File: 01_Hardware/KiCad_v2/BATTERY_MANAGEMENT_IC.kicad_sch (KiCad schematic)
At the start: 36 parts, among them J300 JST_B2B, Q300 BSS314PE, Q301 NVTA7002NT1G, U300 BQ25892

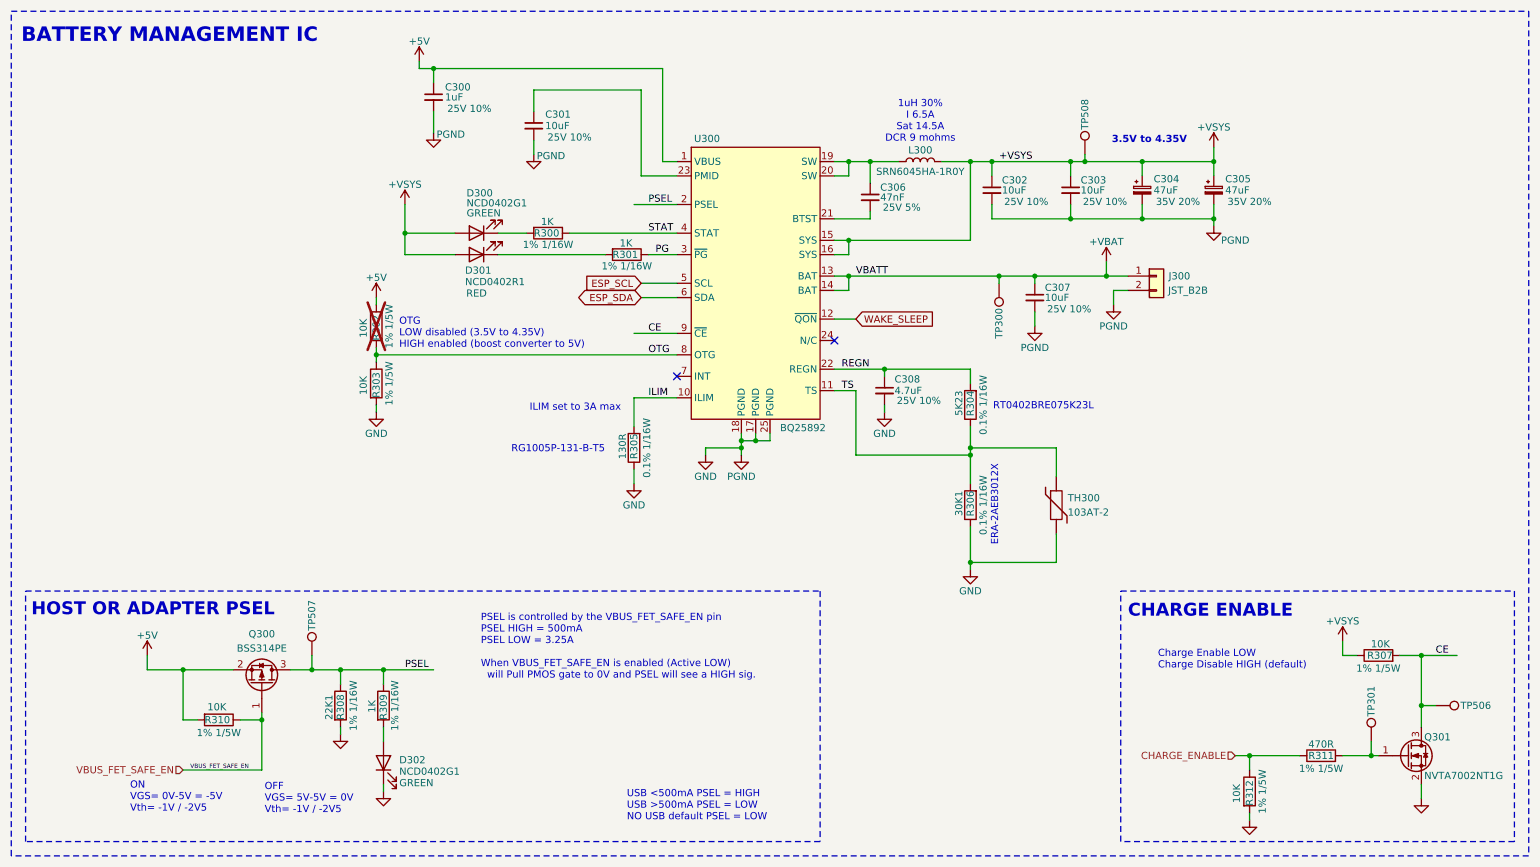
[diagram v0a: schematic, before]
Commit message: BOM done, except connectors/thermistor/button -> Will re-check BOM before sending to manufacturing
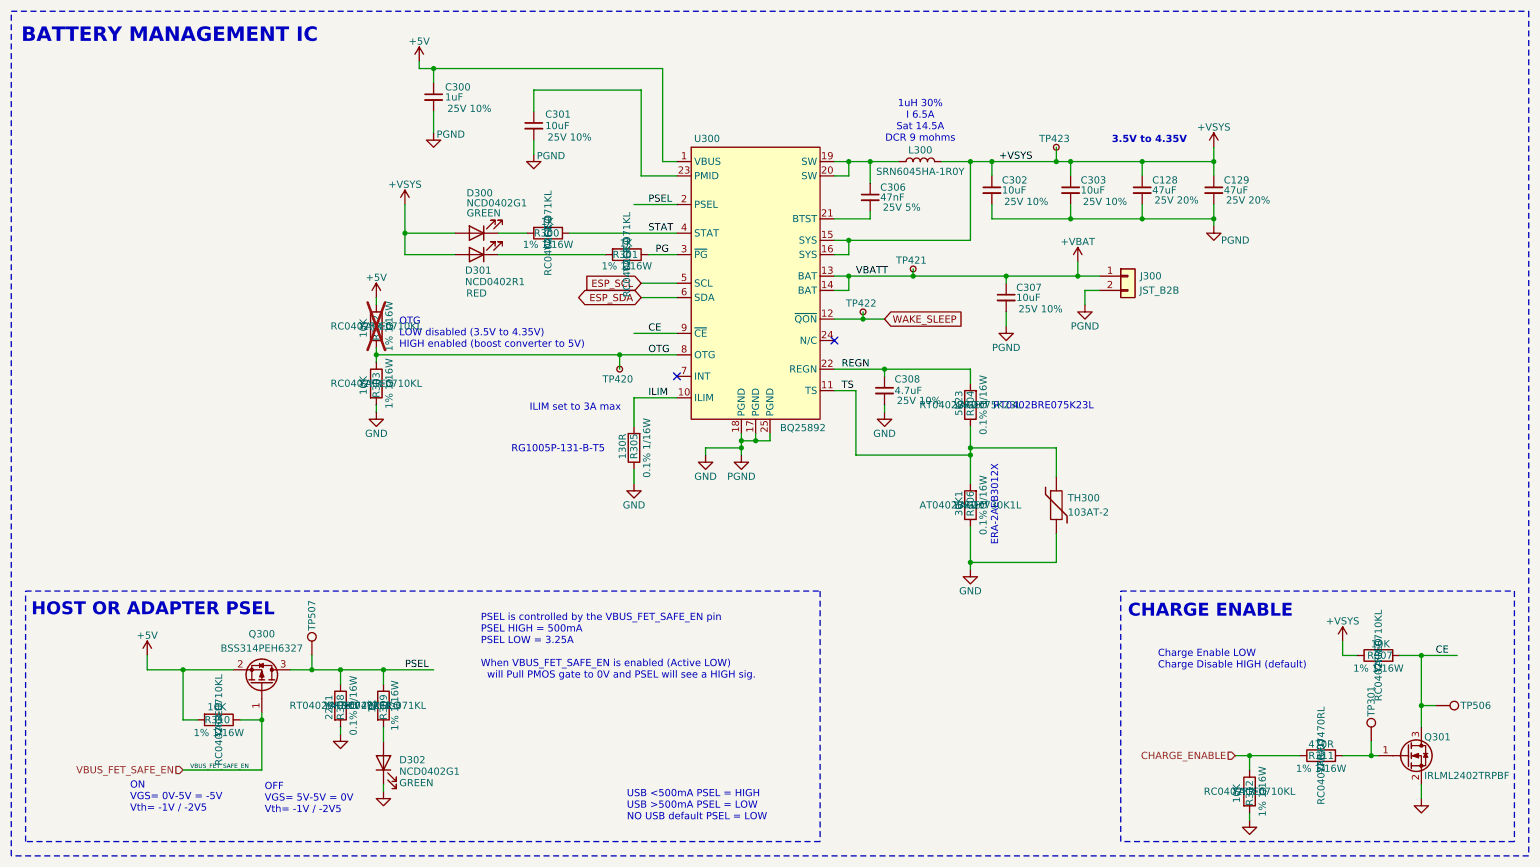
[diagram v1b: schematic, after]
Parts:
- removed C304, C305: 47uF, Capacitor_SMD:CP_Elec_6.3x5.8, symbol Device:C_Polarized_Small
- removed TP300: +VBAT, TestPoint:TestPoint_Pad_D1.0mm, symbol Connector:TestPoint
- removed TP508: ~, TestPoint:TestPoint_Pad_D1.0mm, symbol Connector:TestPoint
- added C128, C129: 47uF, Capacitor_SMD:C_1206_3216Metric, symbol Device:C_Small
- added TP420, TP421, TP422, TP423: TestPoint_Small, TestPoint:TestPoint_Pad_D1.5mm, symbol Connector:TestPoint_Small
- C301, C302, C303, C307: Manufacturer Murata Electronics -> Murata Electronics
- D300, D301, D302: footprint Custom_Global_Footprints:SML-P13PTT_LED_0402_1005Metric -> LED_SMD:LED_0402_1005Metric
- Q300: value BSS314PE -> BSS314PEH6327; Link (none) -> https://jlcpcb.com/partdetail/InfineonTechnologies-BSS314PE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; Manufacturer (none) -> Infineon Technologies; Manufacturer Part Number (none) -> BSS314PEH6327
- Q301: value NVTA7002NT1G -> IRLML2402TRPBF; footprint Custom_Global_Footprints:NVTA7002N -> Package_TO_SOT_SMD:SOT-23; Link (none) -> https://jlcpcb.com/partdetail/InfineonTechnologies-IRLML240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; Manufacturer (none) -> Infineon Technologies; Manufacturer Part Number (none) -> IRLML2402TRPBF
- R300, R301, R309: Manufacturer (none) -> YAGEO; Manufacturer Part Number (none) -> RC0402FR-071KL
- R302, R303, R307, R310, R312: Manufacturer (none) -> YAGEO; Manufacturer Part Number (none) -> RC0402FR-0710KL
- R304: Manufacturer (none) -> YAGEO; Manufacturer Part Number (none) -> RT0402BRD075K23L
- R305: Manufacturer (none) -> YAGEO; Manufacturer Part Number (none) -> RT0402BRD07130RL
- R306: Manufacturer (none) -> YAGEO; Manufacturer Part Number (none) -> AT0402BRD0730K1L
- R308: Manufacturer (none) -> YAGEO; Manufacturer Part Number (none) -> RT0402BRD0722K1L
- R311: Manufacturer (none) -> YAGEO; Manufacturer Part Number (none) -> RC0402FR-07470RL
- U300: Link (none) -> https://jlcpcb.com/partdetail/TexasInstruments-BQ25892RTWR/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; Manufacturer (none) -> Texas Instruments; Manufacturer Part Number (none) -> BQ25892RTWR
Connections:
- net +VBAT: now also TP421.1
- net +VSYS: now also C128.1, C129.1, TP423.1
- net GND: now also C128.2, C129.2
- net OTG: now also TP420.1
- net WAKE_SLEEP: now also TP422.1
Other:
- moved on the sheet: C307, J300

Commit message: USB-C and Serial PCB routing done
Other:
- note removed: "ERA-2AEB3012X"
- note removed: "RT0402BRE075K23L"
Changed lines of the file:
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@@
 		)
 	)
-	(text "RT0402BRE075K23L"
-		(exclude_from_sim no)
-		(at 197.104 84.074 0)
-		(effects
-			(font
-				(size 1.27 1.27)
-			)
-		)
-	)
 	(text "PSEL is controlled by the VBUS_FET_SAFE_EN pin\nPSEL HIGH = 500mA\nPSEL LOW = 3.25A\n\nWhen VBUS_FET_SAFE_EN is enabled (Active LOW)\n  will Pull PMOS gate to 0V and PSEL will see a HIGH sig."
 		(exclude_from_sim no)
@@
 		)
 	)
-	(text "ERA-2AEB3012X"
-		(exclude_from_sim no)
-		(at 188.468 101.6 90)
-		(effects
-			(font
-				(size 1.27 1.27)
-			)
-		)
-	)
 	(text "ON\nVGS= 0V-5V = -5V\nVth= -1V / -2V5"
 		(exclude_from_sim no)
@@
 					(size 1.27 1.27)
 				)
+				(hide yes)
 			)
 		)
@@
 					(size 1.27 1.27)
 				)
+				(hide yes)
 			)
 		)
@@
 					(size 1.27 1.27)
 				)
+				(hide yes)
 			)
 		)
@@
 					(size 1.27 1.27)
 				)
+				(hide yes)
 			)
 		)
@@
 					(size 1.27 1.27)
 				)
+				(hide yes)
 			)
 		)
@@
 					(size 1.27 1.27)
 				)
+				(hide yes)
 			)
 		)
@@
 					(size 1.27 1.27)
 				)
+				(hide yes)
 			)
 		)
@@
 					(size 1.27 1.27)
 				)
+				(hide yes)
 			)
 		)
@@
 					(size 1.27 1.27)
 				)
+				(hide yes)
 			)
 		)
@@
 					(size 1.27 1.27)
 				)
+				(hide yes)
 			)
 		)
@@
 					(size 1.27 1.27)
 				)
+				(hide yes)
 			)
 		)
@@
 					(size 1.27 1.27)
 				)
+				(hide yes)
 			)
 		)
@@
 					(size 1.27 1.27)
 				)
+				(hide yes)
 			)
 		)
@@
 					(size 1.27 1.27)
 				)
+				(hide yes)
 			)
 		)
@@
 					(size 1.27 1.27)
 				)
+				(hide yes)
 			)
 		)
@@
 					(size 1.27 1.27)
 				)
+				(hide yes)
 			)
 		)
@@
 					(size 1.27 1.27)
 				)
+				(hide yes)
 			)
 		)
@@
 					(size 1.27 1.27)
 				)
+				(hide yes)
 			)
 		)
@@
 					(size 1.27 1.27)
 				)
+				(hide yes)
 			)
 		)
@@
 					(size 1.27 1.27)
 				)
+				(hide yes)
 			)
 		)
@@
 					(size 1.27 1.27)
 				)
+				(hide yes)
 			)
 		)
@@
 					(size 1.27 1.27)
 				)
+				(hide yes)
 			)
 		)
@@
 					(size 1.27 1.27)
 				)
+				(hide yes)
 			)
 		)
@@
 					(size 1.27 1.27)
 				)
+				(hide yes)
 			)
 		)
@@
 					(size 1.27 1.27)
 				)
+				(hide yes)
 			)
 		)
@@
 					(size 1.27 1.27)
 				)
+				(hide yes)
 			)
 		)
@@
 					(size 1.27 1.27)
 				)
+				(hide yes)
 			)
 		)
@@
 					(size 1.27 1.27)
 				)
+				(hide yes)
 			)
 		)
@@
 					(size 1.27 1.27)
 				)
+				(hide yes)
 			)
 		)
@@
 					(size 1.27 1.27)
 				)
+				(hide yes)
 			)
 		)
@@
 					(size 1.27 1.27)
 				)
+				(hide yes)
 			)
 		)
@@
 					(size 1.27 1.27)
 				)
+				(hide yes)
 			)
 		)
@@
 					(size 1.27 1.27)
 				)
+				(hide yes)
 			)
 		)
@@
 					(size 1.27 1.27)
 				)
+				(hide yes)
 			)
 		)
@@
 					(size 1.27 1.27)
 				)
+				(hide yes)
 			)
 		)
@@
 					(size 1.27 1.27)
 				)
+				(hide yes)
 			)
 		)
@@
 					(size 1.27 1.27)
 				)
+				(hide yes)
 			)
 		)
@@
 					(size 1.27 1.27)
 				)
+				(hide yes)
 			)
 		)
@@
 					(size 1.27 1.27)
 				)
+				(hide yes)
 			)
 		)
@@
 					(size 1.27 1.27)
 				)
+				(hide yes)
 			)
 		)
@@
 					(size 1.27 1.27)
 				)
+				(hide yes)
 			)
 		)
@@
 					(size 1.27 1.27)
 				)
+				(hide yes)
 			)
 		)
@@
 					(size 1.27 1.27)
 				)
+				(hide yes)
 			)
 		)
@@
 					(size 1.27 1.27)
 				)
+				(hide yes)
 			)
 		)
@@
 					(size 1.27 1.27)
 				)
+				(hide yes)
 			)
 		)
@@
 					(size 1.27 1.27)
 				)
+				(hide yes)
 			)
 		)
@@
 					(size 1.27 1.27)
 				)
+				(hide yes)
 			)
 		)
@@
 					(size 1.27 1.27)
 				)
+				(hide yes)
 			)
 		)
@@
 					(size 1.27 1.27)
 				)
+				(hide yes)
 			)
 		)
@@
 					(size 1.27 1.27)
 				)
+				(hide yes)
 			)
 		)
@@
 					(size 1.27 1.27)
 				)
+				(hide yes)
 			)
 		)
@@
 					(size 1.27 1.27)
 				)
+				(hide yes)
 			)
 		)
@@
 					(size 1.27 1.27)
 				)
+				(hide yes)
 			)
 		)
@@
 					(size 1.27 1.27)
 				)
+				(hide yes)
 			)
 		)
@@
 					(size 1.27 1.27)
 				)
+				(hide yes)
 			)
 		)

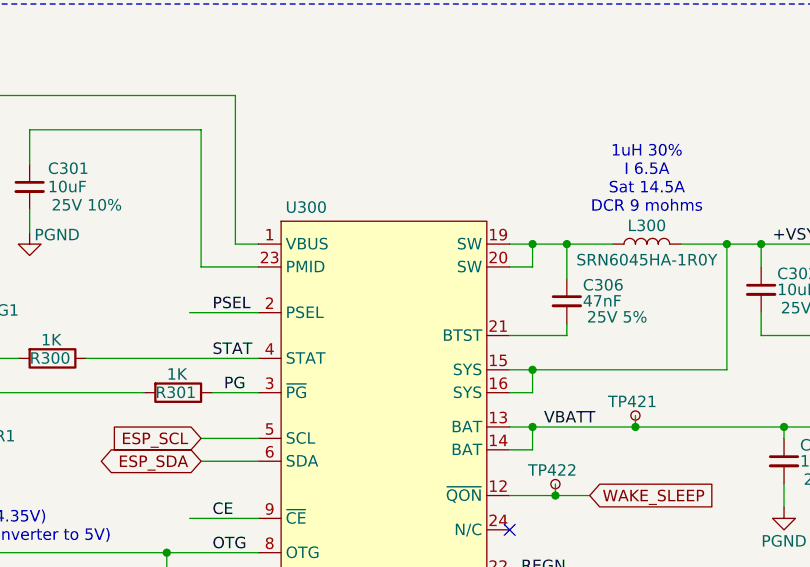
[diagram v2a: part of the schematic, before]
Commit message: Power plane/rearranged connectors
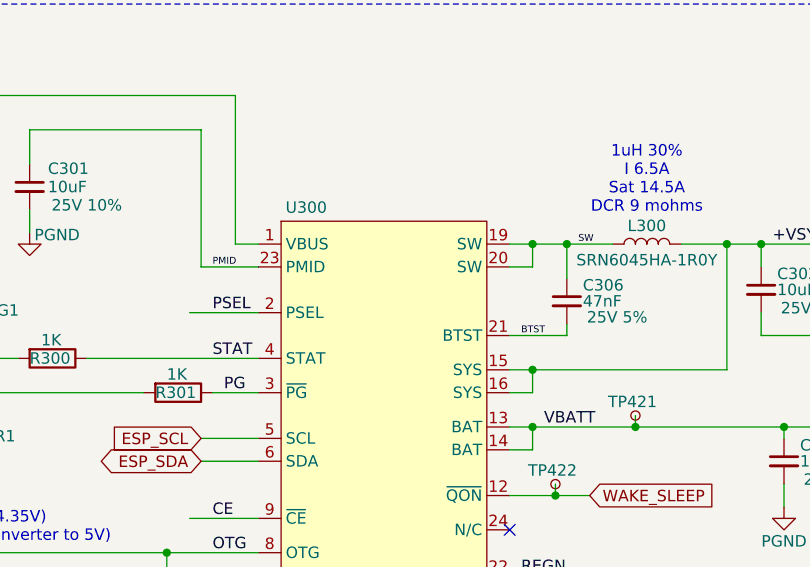
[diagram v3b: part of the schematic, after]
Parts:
- TH300: footprint Connector_PinSocket_2.54mm:PinSocket_1x02_P2.54mm_Vertical -> Connector_PinHeader_2.54mm:PinHeader_1x02_P2.54mm_Vertical
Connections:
- net PMID: now reaches C301.1, U300.23 (PMID)
- net SW: now reaches C306.1, L300.1, U300.19 (SW), U300.20 (SW)
- net BTST: now reaches C306.2, U300.21 (BTST)
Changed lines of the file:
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@@
+		)
+	)
+	(label "PMID"
+		(at 127 43.18 0)
+		(effects
+			(font
+				(size 0.762 0.762)
+			)
+			(justify left bottom)
 		)
 	)
@@
 		)
 	)
+	(label "BTST"
+		(at 161.29 50.8 0)
+		(effects
+			(font
+				(size 0.762 0.762)
+			)
+			(justify left bottom)
+		)
+	)
 	(label "CE"
 		(at 127 71.12 0)
@@
 			(font
 				(size 1.27 1.27)
+			)
+			(justify left bottom)
+		)
+	)
+	(label "SW"
+		(at 167.64 40.64 0)
+		(effects
+			(font
+				(size 0.762 0.762)
 			)
 			(justify left bottom)
@@
 			)
 		)
-		(property "Footprint" "Connector_PinSocket_2.54mm:PinSocket_1x02_P2.54mm_Vertical"
+		(property "Footprint" "Connector_PinHeader_2.54mm:PinHeader_1x02_P2.54mm_Vertical"
 			(at 199.39 101.6 0)
 			(effects

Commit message: Hardware for manufacturing v0.2
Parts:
- C308: Manufacturer Samsung Electro-Mechanics -> (none); Manufacturer Part Number CL10A475KA8NQNC -> (none)
- R310: now not fitted; now left out of the parts list
- TP420, TP421, TP422, TP423: footprint TestPoint:TestPoint_Pad_D1.5mm -> TestPoint:TestPoint_Pad_D1.0mm
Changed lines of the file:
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@@
 					(size 1.27 1.27)
 				)
-				(hide yes)
 			)
 		)
@@
 			)
 		)
-		(property "Footprint" "TestPoint:TestPoint_Pad_D1.5mm"
+		(property "Footprint" "TestPoint:TestPoint_Pad_D1.0mm"
 			(at 170.18 67.31 0)
 			(effects
@@
 					(size 1.27 1.27)
 				)
-				(hide yes)
 			)
 		)
@@
 			)
 		)
-		(property "Footprint" "TestPoint:TestPoint_Pad_D1.5mm"
+		(property "Footprint" "TestPoint:TestPoint_Pad_D1.0mm"
 			(at 127 77.47 0)
 			(effects
@@
 			)
 		)
-		(property "Footprint" "TestPoint:TestPoint_Pad_D1.5mm"
+		(property "Footprint" "TestPoint:TestPoint_Pad_D1.0mm"
 			(at 204.47 38.1 0)
 			(effects
@@
 		(unit 1)
 		(exclude_from_sim no)
-		(in_bom yes)
+		(in_bom no)
 		(on_board yes)
-		(dnp no)
+		(dnp yes)
 		(property "Reference" "R310"
 			(at 48.26 139.7 90)
@@
 					(size 1.27 1.27)
 				)
-				(hide yes)
 			)
 		)
@@
 					(size 1.27 1.27)
 				)
-				(hide yes)
 			)
 		)
@@
 					(size 1.27 1.27)
 				)
-				(hide yes)
 			)
 		)
@@
 			)
 		)
-		(property "Footprint" "TestPoint:TestPoint_Pad_D1.5mm"
+		(property "Footprint" "TestPoint:TestPoint_Pad_D1.0mm"
 			(at 179.07 59.69 0)
 			(effects
@@
 					(size 1.27 1.27)
 				)
-				(hide yes)
 			)
 		)
@@
 					(size 1.27 1.27)
 				)
-				(hide yes)
 			)
 		)
@@
 			)
 		)
-		(property "Datasheet" "https://jlcpcb.com/api/file/downloadByFileSystemAccessId/8586178720680333312"
+		(property "Datasheet" ""
 			(at 168.91 81.28 0)
 			(effects
@@
 			)
 		)
-		(property "Manufacturer" "Samsung Electro-Mechanics "
+		(property "Manufacturer" ""
 			(at 168.91 81.28 0)
 			(effects
@@
 			)
 		)
-		(property "Manufacturer Part Number" "CL10A475KA8NQNC"
+		(property "Manufacturer Part Number" ""
 			(at 168.91 81.28 0)
 			(effects
